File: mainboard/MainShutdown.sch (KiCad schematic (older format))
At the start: 23 parts, among them J10 CONN_2X2, J6 CONN_2X2, K1 KT12-1A, K2 G6DN 12V, Q1 NTR4003N, Q2 TSM2312, U13 TS3704IPT, U14 CD4044, U15 CD4082, U4 MainBoard_AD8244

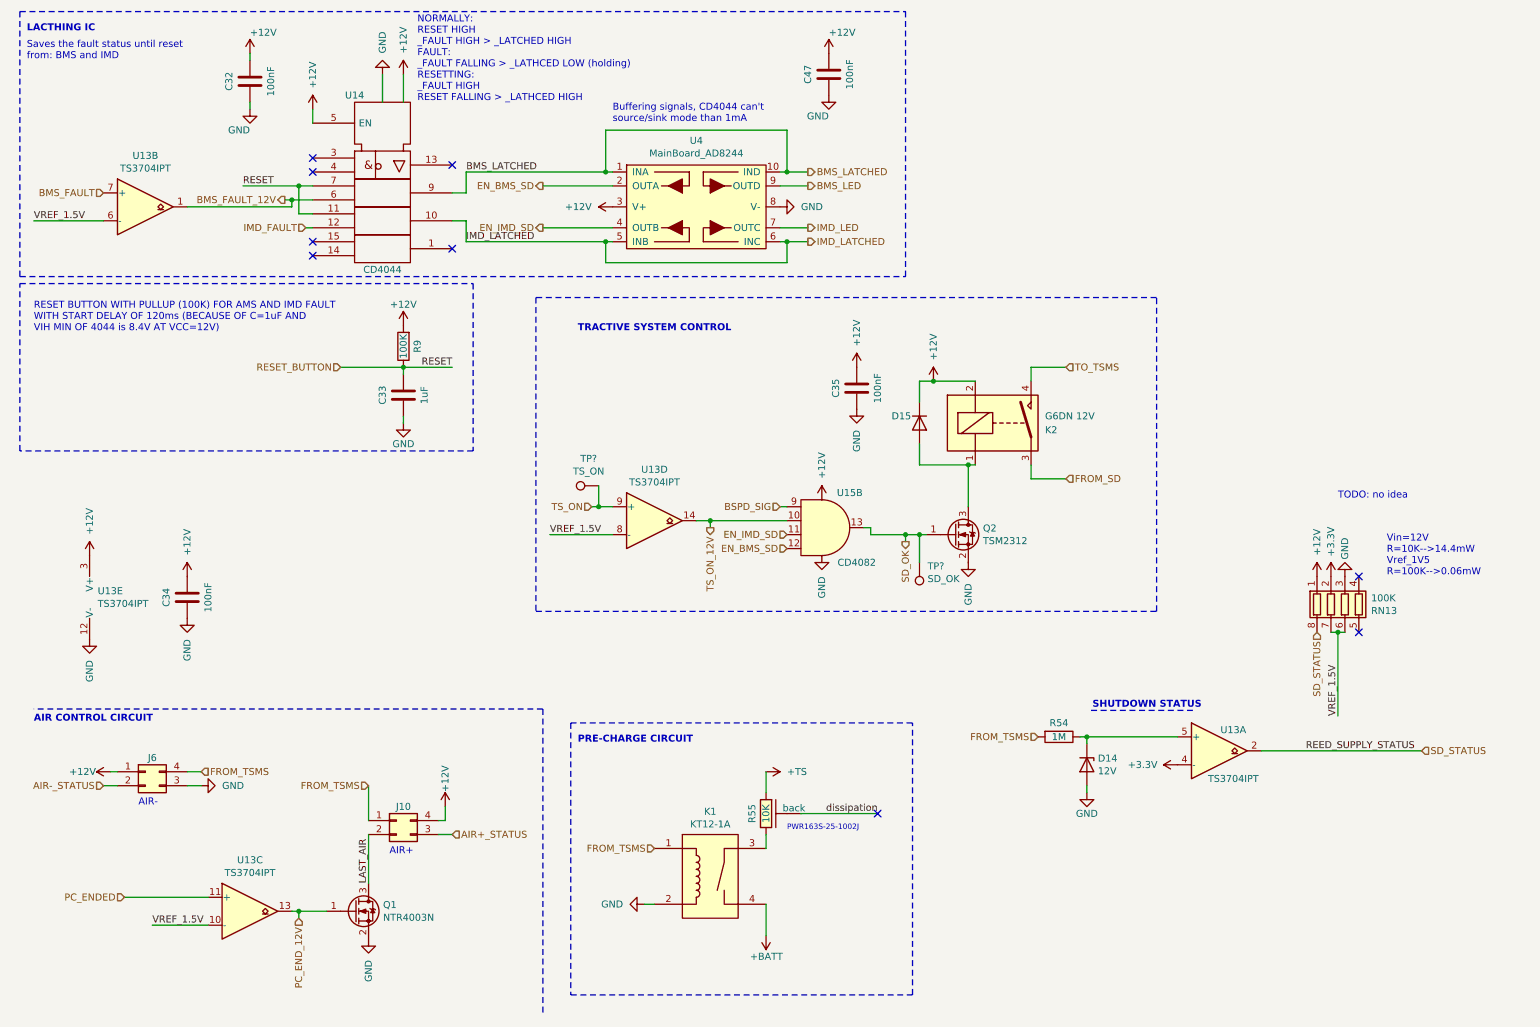
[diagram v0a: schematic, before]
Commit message: adding testpoints
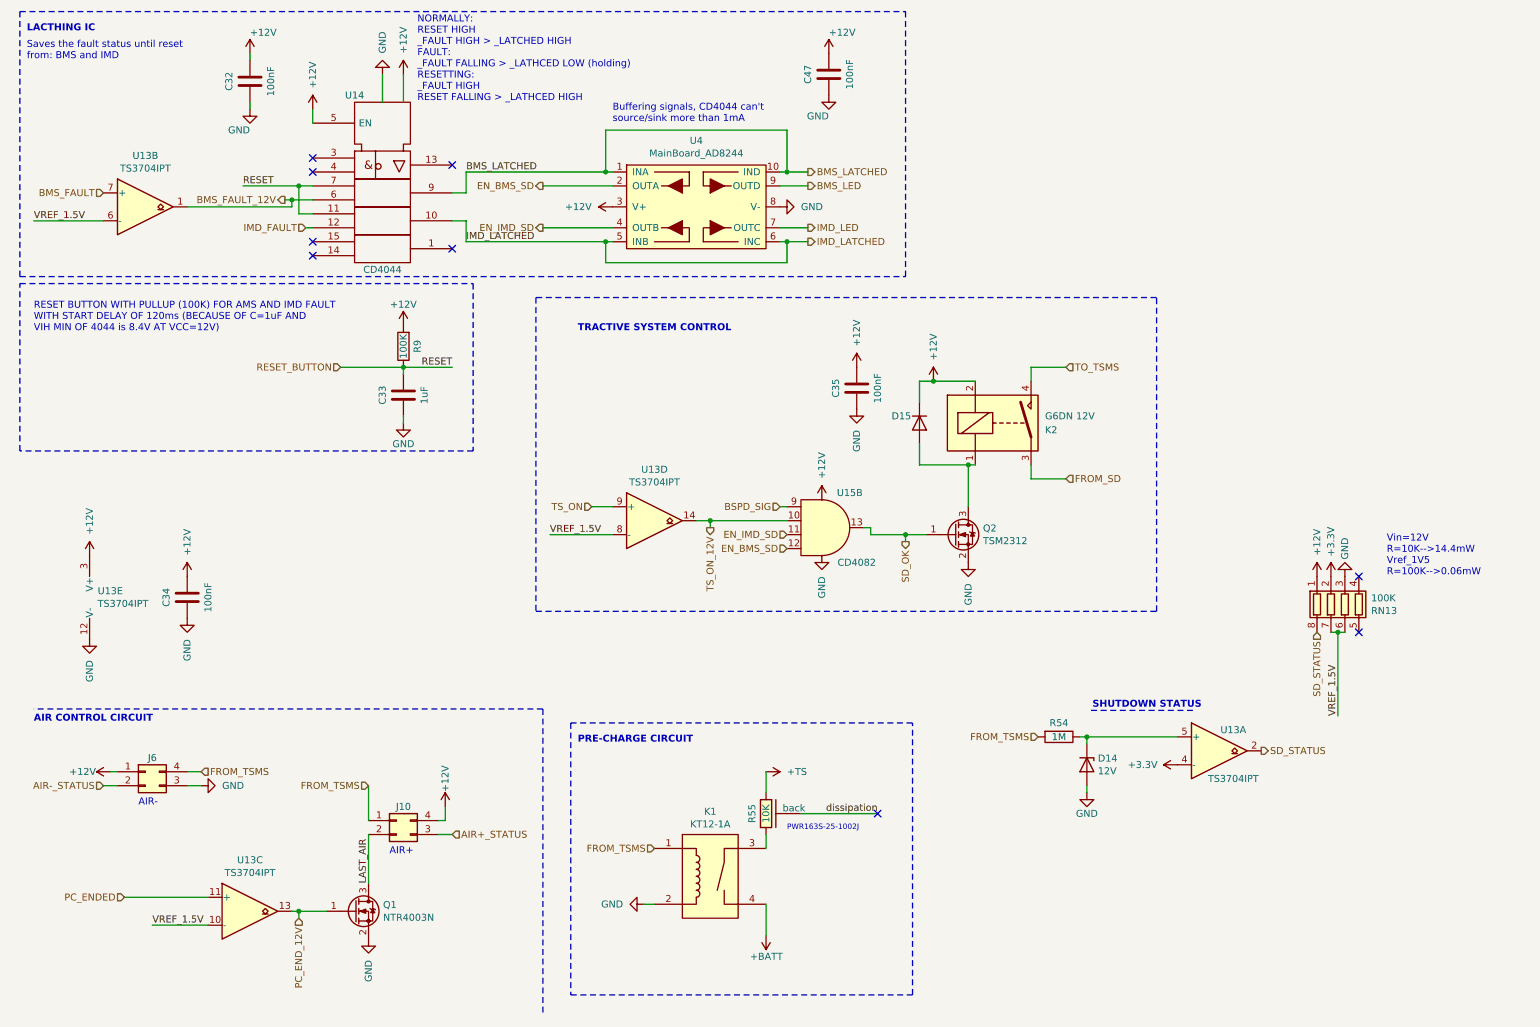
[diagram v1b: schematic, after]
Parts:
- removed TP?: SD_OK, symbol Connector:TestPoint
- removed TP?: TS_ON, symbol Connector:TestPoint
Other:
- note added: "Buffering signals, CD4044 can't \nsource/sink more than 1mA"
- note removed: "Buffering signals, CD4044 can't \nsource/sink mode than 1mA"
- note removed: "TODO: no idea"
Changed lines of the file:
@@
 Connection ~ 6850 4250
-Wire Wire Line
-	6850 4250 6950 4250
 Wire Wire Line
 	6600 4250 6850 4250
@@
 	1    0    0    -1
 $EndComp
-Text HLabel 10550 5800 2    50   Input ~ 0
+Text HLabel 9400 5800 2    50   Output ~ 0
 SD_STATUS
-Text Label 10500 5800 2    50   ~ 0
-REED_SUPPLY_STATUS
 $Comp
 L power:+12V #PWR?
@@
 $EndComp
 Wire Wire Line
-	9400 5800 10550 5800
-Wire Wire Line
 	2500 6950 2700 6950
 Text Notes 550  850  0    50   ~ 0
@@
 	1    0    0    -1
 $EndComp
-Text Notes 9950 4000 0    50   ~ 0
-TODO: no idea
 Text Notes 4750 1300 0    50   ~ 0
-Buffering signals, CD4044 can't \nsource/sink mode than 1mA
+Buffering signals, CD4044 can't \nsource/sink more than 1mA
 Wire Wire Line
 	5950 1750 6150 1750
@@
 Wire Notes Line
 	4250 5500 4250 7700
-$Comp
-L Connector:TestPoint TP?
-U 1 1 6059EB75
-P 6950 4450
-F 0 "TP?" H 6892 4476 50  0000 R CNN
-F 1 "SD_OK" H 6892 4567 50  0000 R CNN
-F 2 "" H 7150 4450 50  0001 C CNN
-F 3 "~" H 7150 4450 50  0001 C CNN
-	1    6950 4450
-	-1   0    0    1
-$EndComp
-Wire Wire Line
-	6950 4450 6950 4250
-Connection ~ 6950 4250
-Wire Wire Line
-	6950 4250 7000 4250
-$Comp
-L Connector:TestPoint TP?
-U 1 1 605A3994
-P 4650 3900
-F 0 "TP?" V 4845 3972 50  0000 C CNN
-F 1 "TS_ON" V 4754 3972 50  0000 C CNN
-F 2 "" H 4850 3900 50  0001 C CNN
-F 3 "~" H 4850 3900 50  0001 C CNN
-	1    4650 3900
-	0    -1   -1   0
-$EndComp
-Wire Wire Line
-	4600 4050 4650 4050
-Wire Wire Line
-	4650 3900 4650 4050
-Connection ~ 4650 4050
-Wire Wire Line
-	4650 4050 4750 4050
 Wire Wire Line
 	1150 5950 1200 5950
@@
 EndData
 $EndBitmap
+Wire Wire Line
+	6850 4250 7000 4250
+Wire Wire Line
+	4600 4050 4750 4050
 $EndSCHEMATC

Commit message: changed Q2
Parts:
- removed Q2: TSM2312, Package_TO_SOT_SMD:TSOT-23, symbol Device:Q_NMOS_GSD
- added Q?: NTR4003N, Package_TO_SOT_SMD:SOT-23, symbol Device:Q_NMOS_GSD
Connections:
- net GND: now also Q?.2 (S)
- net SD_OK: now also Q?.1 (G)
- net at D15.2 (A), K2.1: now also Q?.3 (D)
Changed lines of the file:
@@
 	4600 4050 4750 4050
 $Comp
-L Device:Q_NMOS_GSD Q2
-U 1 1 5E40BAFD
+L Device:Q_NMOS_GSD Q?
+U 1 1 605E5D5D
 P 7200 4250
-F 0 "Q2" H 7405 4296 50  0000 L CNN
-F 1 "TSM2312" H 7405 4205 50  0000 L CNN
-F 2 "Package_TO_SOT_SMD:TSOT-23" H 7400 4350 50  0001 C CNN
-F 3 "~" H 7200 4250 50  0001 C CNN
+F 0 "Q?" H 7404 4296 50  0000 L CNN
+F 1 "NTR4003N" H 7404 4205 50  0000 L CNN
+F 2 "Package_TO_SOT_SMD:SOT-23" H 7400 4350 50  0001 C CNN
+F 3 "https://www.mouser.it/ProductDetail/Toshiba/SSM3K361TULF?qs=sGAEpiMZZMshyDBzk1%2FWi%2FD7Em5shE8qqtsfXGfVhuGHqmGZGu2Z8A%3D%3D" H 7200 4250 50  0001 C CNN
 	1    7200 4250
 	1    0    0    -1

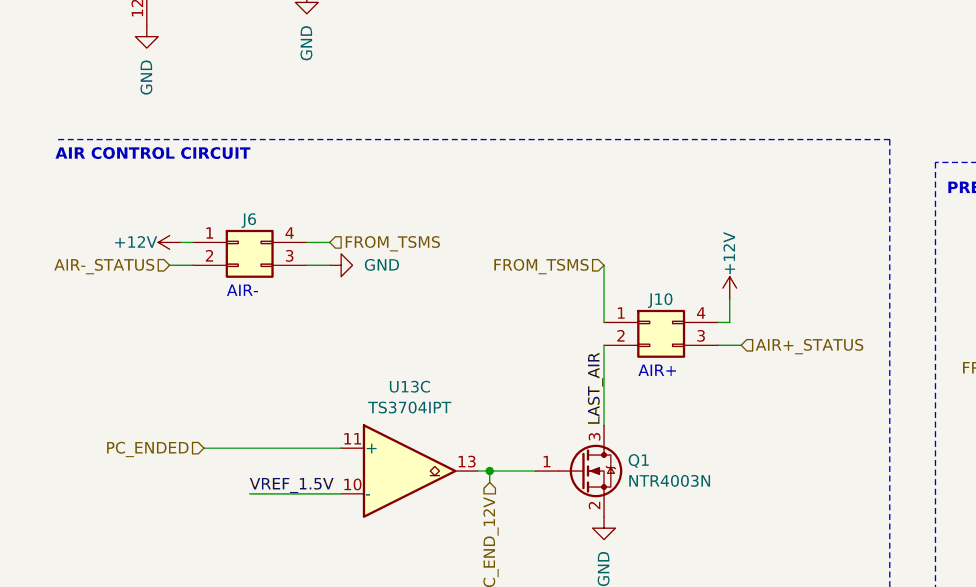
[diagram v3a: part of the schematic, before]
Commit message: redone the air connections for clarity
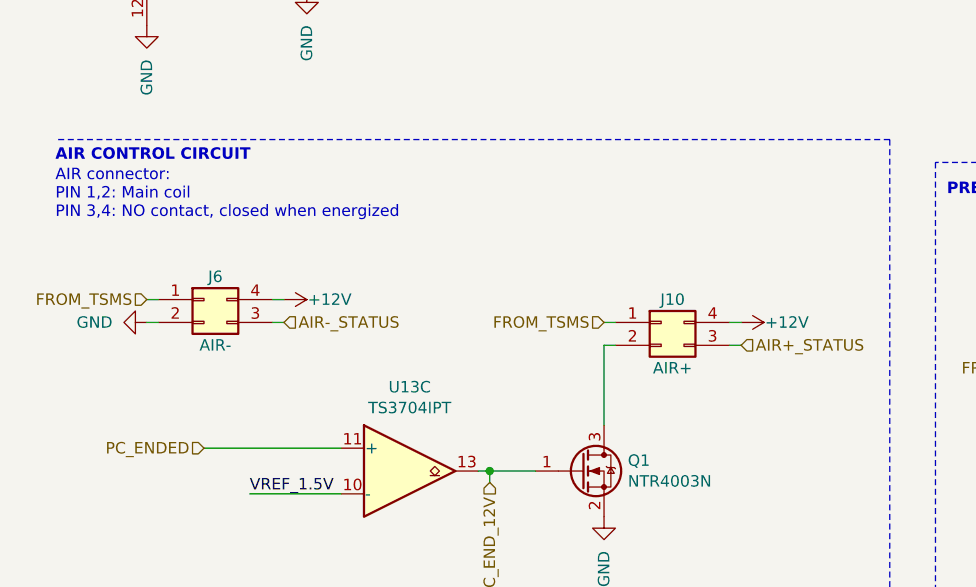
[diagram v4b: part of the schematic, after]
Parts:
- J10: value CONN_2X2 -> AIR+
- J6: value CONN_2X2 -> AIR-
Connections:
- net +12V: now also J6.4 (Pin_4); no longer J6.1 (Pin_1)
- net AIR-_STATUS: now also J6.3 (Pin_3); no longer J6.2 (Pin_2)
- net FROM_TSMS: now also J6.1 (Pin_1); no longer J6.4 (Pin_4)
- net GND: now also J6.2 (Pin_2); no longer J6.3 (Pin_3)
- net LAST_AIR: no longer names the net of J10.2 (Pin_2), Q1.3 (D)
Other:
- note added: "AIR connector:\nPIN 1,2: Main coil\nPIN 3,4: NO contact, closed when energized"
- note removed: "AIR+"
- note removed: "AIR-"
- moved on the sheet: J10, J6
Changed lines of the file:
@@
 $EndComp
 Wire Wire Line
-	3550 6200 3550 6300
-Wire Wire Line
-	3550 6300 3500 6300
+	3600 6300 3550 6300
 $Comp
 L MainBoard:R_power_backplane R55
@@
 L power:+12V #PWR?
 U 1 1 5E2DE393
-P 3550 6200
+P 3600 6300
 AR Path="/5E2DE393" Ref="#PWR?"  Part="1"
 AR Path="/5B045B0D/5E2DE393" Ref="#PWR0136"  Part="1"
-F 0 "#PWR0136" H 3550 6050 50  0001 C CNN
-F 1 "+12V" V 3550 6400 50  0000 C CNN
-F 2 "" H 3550 6200 50  0001 C CNN
-F 3 "" H 3550 6200 50  0001 C CNN
-	1    3550 6200
-	1    0    0    -1
+F 0 "#PWR0136" H 3600 6150 50  0001 C CNN
+F 1 "+12V" V 3600 6500 50  0000 C CNN
+F 2 "" H 3600 6300 50  0001 C CNN
+F 3 "" H 3600 6300 50  0001 C CNN
+	1    3600 6300
+	0    1    1    0
 $EndComp
 $Comp
 L power:+12V #PWR?
 U 1 1 5E2E4AFA
-P 1150 5950
+P 1600 6200
 AR Path="/5E2E4AFA" Ref="#PWR?"  Part="1"
 AR Path="/5B045B0D/5E2E4AFA" Ref="#PWR0140"  Part="1"
-F 0 "#PWR0140" H 1150 5800 50  0001 C CNN
-F 1 "+12V" V 1150 6150 50  0000 C CNN
-F 2 "" H 1150 5950 50  0001 C CNN
-F 3 "" H 1150 5950 50  0001 C CNN
-	1    1150 5950
-	0    -1   -1   0
+F 0 "#PWR0140" H 1600 6050 50  0001 C CNN
+F 1 "+12V" V 1600 6400 50  0000 C CNN
+F 2 "" H 1600 6200 50  0001 C CNN
+F 3 "" H 1600 6200 50  0001 C CNN
+	1    1600 6200
+	0    1    -1   0
 $EndComp
 Text HLabel 3600 6400 2    50   Input ~ 0
 AIR+_STATUS
-Text HLabel 1100 6050 0    50   Input ~ 0
+Text HLabel 1600 6300 2    50   Input ~ 0
 AIR-_STATUS
 Text Label 6650 6250 2    50   ~ 0
@@
 Text Notes 600  5600 0    50   ~ 10
 AIR CONTROL CIRCUIT\n
-Text HLabel 3000 6050 0    50   Input ~ 0
+Text HLabel 3000 6300 0    50   Input ~ 0
 FROM_TSMS
 Text HLabel 1250 6850 0    50   Input ~ 0
@@
 Wire Wire Line
 	2450 6950 2500 6950
-$Comp
-L power:GND #PWR0135
-U 1 1 5B0DE170
-P 1800 6050
-F 0 "#PWR0135" H 1800 5800 50  0001 C CNN
-F 1 "GND" V 1800 5900 50  0000 R CNN
-F 2 "" H 1800 6050 50  0001 C CNN
-F 3 "" H 1800 6050 50  0001 C CNN
-	1    1800 6050
-	0    -1   -1   0
-$EndComp
-Wire Wire Line
-	1700 5950 1800 5950
-Wire Wire Line
-	1800 6050 1700 6050
-Text HLabel 1800 5950 2    50   Input ~ 0
-FROM_TSMS
 Wire Wire Line
 	3000 6400 3000 6750
@@
 	7300 3750 6950 3750
 $Comp
-L power:GND #PWR0151
-U 1 1 5E40D944
-P 7300 4450
-F 0 "#PWR0151" H 7300 4200 50  0001 C CNN
-F 1 "GND" V 7300 4300 50  0000 R CNN
-F 2 "" H 7300 4450 50  0001 C CNN
-F 3 "" H 7300 4450 50  0001 C CNN
-	1    7300 4450
-	1    0    0    -1
-$EndComp
-$Comp
 L power:+12V #PWR?
 U 1 1 5E40DC05
@@
 	8150 6050 8150 6100
 Wire Wire Line
-	3500 6400 3600 6400
-Wire Wire Line
-	1200 6050 1100 6050
+	3550 6400 3600 6400
 Wire Notes Line
 	3750 2450 3750 3650
@@
 	1    0    0    -1
 $EndComp
-Text Label 3000 6750 1    50   ~ 0
-LAST_AIR
-Wire Wire Line
-	3000 6050 3000 6300
 $Comp
 L Connector_Generic:Conn_02x02_Counter_Clockwise J?
 U 1 1 5E5EF8A6
-P 3200 6300
+P 3250 6300
 AR Path="/5B50ED38/5E5EF8A6" Ref="J?"  Part="1"
 AR Path="/5B045B0D/5E5EF8A6" Ref="J10"  Part="1"
-F 0 "J10" H 3250 6400 50  0000 C CNN
-F 1 "CONN_2X2" H 3250 6426 50  0001 C CNN
-F 2 "MainBoard:Molex_Micro-Fit_3.0_43045-0412_2x02_P3.00mm_Vertical" H 3200 6300 50  0001 C CNN
-F 3 "~" H 3200 6300 50  0001 C CNN
-	1    3200 6300
+F 0 "J10" H 3300 6400 50  0000 C CNN
+F 1 "AIR+" H 3300 6100 50  0000 C CNN
+F 2 "MainBoard:Molex_Micro-Fit_3.0_43045-0412_2x02_P3.00mm_Vertical" H 3250 6300 50  0001 C CNN
+F 3 "~" H 3250 6300 50  0001 C CNN
+	1    3250 6300
 	1    0    0    -1
 $EndComp
@@
 L Connector_Generic:Conn_02x02_Counter_Clockwise J?
 U 1 1 5E5D4844
-P 1400 5950
+P 1250 6200
 AR Path="/5B50ED38/5E5D4844" Ref="J?"  Part="1"
 AR Path="/5B045B0D/5E5D4844" Ref="J6"  Part="1"
-F 0 "J6" H 1450 6050 50  0000 C CNN
-F 1 "CONN_2X2" H 1450 6076 50  0001 C CNN
-F 2 "MainBoard:Molex_Micro-Fit_3.0_43045-0412_2x02_P3.00mm_Vertical" H 1400 5950 50  0001 C CNN
-F 3 "~" H 1400 5950 50  0001 C CNN
-	1    1400 5950
+F 0 "J6" H 1300 6300 50  0000 C CNN
+F 1 "AIR-" H 1300 6000 50  0000 C CNN
+F 2 "MainBoard:Molex_Micro-Fit_3.0_43045-0412_2x02_P3.00mm_Vertical" H 1250 6200 50  0001 C CNN
+F 3 "~" H 1250 6200 50  0001 C CNN
+	1    1250 6200
 	1    0    0    -1
 $EndComp
@@
 Text Notes 10300 4550 0    50   ~ 0
 Vin=12V\nR=10K-->14.4mW\nVref_1V5\nR=100K-->0.06mW
-Text Notes 3150 6550 0    50   ~ 0
-AIR+
-Text Notes 1350 6200 0    50   ~ 0
-AIR-
 $Comp
 L MainBoard:CD4082 U15
@@
 	4250 5500 4250 7700
 Wire Wire Line
-	1150 5950 1200 5950
+	1600 6200 1550 6200
 Wire Wire Line
 	4250 2050 4750 2050
@@
 	1    0    0    -1
 $EndComp
+$Comp
+L power:GND #PWR0151
+U 1 1 5E40D944
+P 7300 4450
+F 0 "#PWR0151" H 7300 4200 50  0001 C CNN
+F 1 "GND" V 7300 4300 50  0000 R CNN
+F 2 "" H 7300 4450 50  0001 C CNN
+F 3 "" H 7300 4450 50  0001 C CNN
+	1    7300 4450
+	1    0    0    -1
+$EndComp
+Text Notes 600  5850 0    50   ~ 0
+AIR connector:\nPIN 1,2: Main coil\nPIN 3,4: NO contact, closed when energized
+Text HLabel 1000 6200 0    50   Input ~ 0
+FROM_TSMS
+$Comp
+L power:GND #PWR0135
+U 1 1 5B0DE170
+P 1000 6300
+F 0 "#PWR0135" H 1000 6050 50  0001 C CNN
+F 1 "GND" V 1000 6150 50  0000 R CNN
+F 2 "" H 1000 6300 50  0001 C CNN
+F 3 "" H 1000 6300 50  0001 C CNN
+	1    1000 6300
+	0    1    -1   0
+$EndComp
+Wire Wire Line
+	1000 6300 1050 6300
+Wire Wire Line
+	1050 6200 1000 6200
+Wire Wire Line
+	1600 6300 1550 6300
+Wire Wire Line
+	3000 6400 3050 6400
+Wire Wire Line
+	3050 6300 3000 6300
 $EndSCHEMATC
